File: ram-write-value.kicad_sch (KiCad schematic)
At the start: 13 parts, among them SW4 SW_DIP_x08, U31 74HCT157

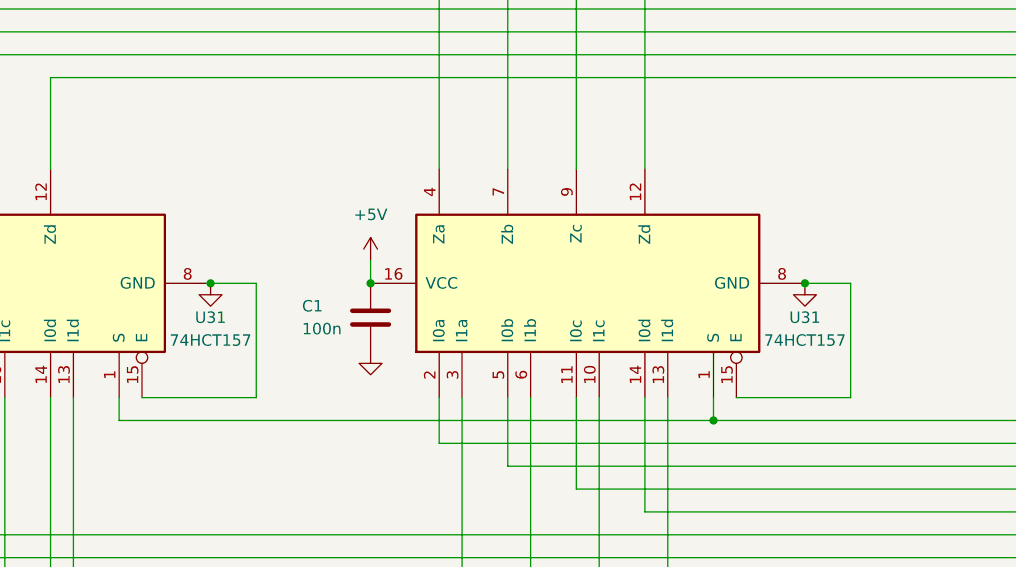
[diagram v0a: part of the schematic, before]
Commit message: added stack and x register.  Added logic for stack_address so ram address 7 gets passes and ram address 8 is high
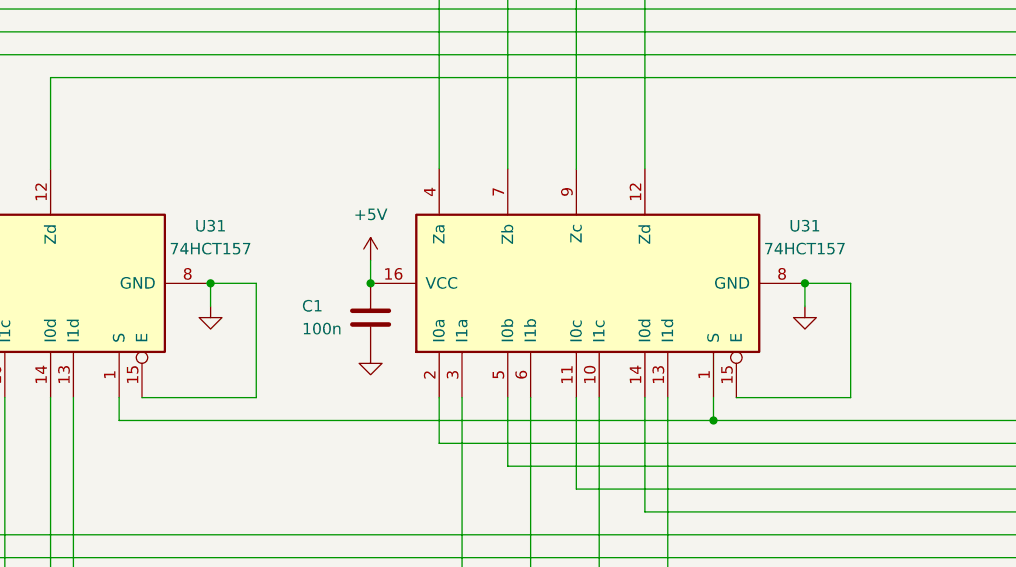
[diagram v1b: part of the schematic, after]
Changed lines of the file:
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@@
     (stroke (width 0) (type default) (color 0 0 255 1))
+  )
+  (wire (pts (xy 134.62 60.96) (xy 134.62 58.42))
+    (stroke (width 0) (type default))
+  )
+  (wire (pts (xy 200.66 60.96) (xy 200.66 58.42))
+    (stroke (width 0) (type default))
   )
   (wire (pts (xy 205.74 58.42) (xy 200.66 58.42))
@@
     )
   )
-  (symbol (lib_id "power:GND") (at 134.62 58.42 0) (unit 1)
+  (symbol (lib_id "power:GND") (at 134.62 60.96 0) (unit 1)
     (in_bom yes) (on_board yes) (dnp no) (fields_autoplaced)
-    (property "Reference" "#PWR03" (at 134.62 64.77 0)
-      (effects (font (size 1.27 1.27)) hide)
-    )
-    (property "Value" "GND" (at 134.62 63.5 0)
-      (effects (font (size 1.27 1.27)) hide)
-    )
-    (property "Footprint" "" (at 134.62 58.42 0)
-      (effects (font (size 1.27 1.27)) hide)
-    )
-    (property "Datasheet" "" (at 134.62 58.42 0)
+    (property "Reference" "#PWR03" (at 134.62 67.31 0)
+      (effects (font (size 1.27 1.27)) hide)
+    )
+    (property "Value" "GND" (at 134.62 66.04 0)
+      (effects (font (size 1.27 1.27)) hide)
+    )
+    (property "Footprint" "" (at 134.62 60.96 0)
+      (effects (font (size 1.27 1.27)) hide)
+    )
+    (property "Datasheet" "" (at 134.62 60.96 0)
       (effects (font (size 1.27 1.27)) hide)
     )
@@
   (symbol (lib_id "74xx:74LS157") (at 109.22 58.42 90) (unit 1)
     (in_bom yes) (on_board yes) (dnp no)
-    (property "Reference" "U31" (at 134.62 62.23 90)
+    (property "Reference" "U31" (at 134.62 52.07 90)
       (effects (font (size 1.27 1.27)))
     )
-    (property "Value" "74HCT157" (at 134.62 64.77 90)
+    (property "Value" "74HCT157" (at 134.62 54.61 90)
       (effects (font (size 1.27 1.27)))
     )
@@
   (symbol (lib_id "74xx:74LS157") (at 175.26 58.42 90) (unit 1)
     (in_bom yes) (on_board yes) (dnp no)
-    (property "Reference" "U31" (at 200.66 62.23 90)
+    (property "Reference" "U31" (at 200.66 52.07 90)
       (effects (font (size 1.27 1.27)))
     )
-    (property "Value" "74HCT157" (at 200.66 64.77 90)
+    (property "Value" "74HCT157" (at 200.66 54.61 90)
       (effects (font (size 1.27 1.27)))
     )
@@
     )
   )
-  (symbol (lib_id "power:GND") (at 200.66 58.42 0) (unit 1)
+  (symbol (lib_id "power:GND") (at 200.66 60.96 0) (unit 1)
     (in_bom yes) (on_board yes) (dnp no) (fields_autoplaced)
-    (property "Reference" "#PWR03" (at 200.66 64.77 0)
-      (effects (font (size 1.27 1.27)) hide)
-    )
-    (property "Value" "GND" (at 200.66 63.5 0)
-      (effects (font (size 1.27 1.27)) hide)
-    )
-    (property "Footprint" "" (at 200.66 58.42 0)
-      (effects (font (size 1.27 1.27)) hide)
-    )
-    (property "Datasheet" "" (at 200.66 58.42 0)
-      (effects (font (size 1.27 1.27)) hide)
-    )
+    (property "Reference" "#PWR03" (at 200.66 67.31 0)
+      (effects (font (size 1.27 1.27)) hide)
+    )
+    (property "Value" "GND" (at 200.66 66.04 0)
+      (effects (font (size 1.27 1.27)) hide)
+    )
+    (property "Footprint" "" (at 200.66 60.96 0)
+      (effects (font (size 1.27 1.27)) hide)
+    )
+    (property "Datasheet" "" (at 200.66 60.96 0)
+      (effects (font (size 1.27 1.27)) hide)
+    )

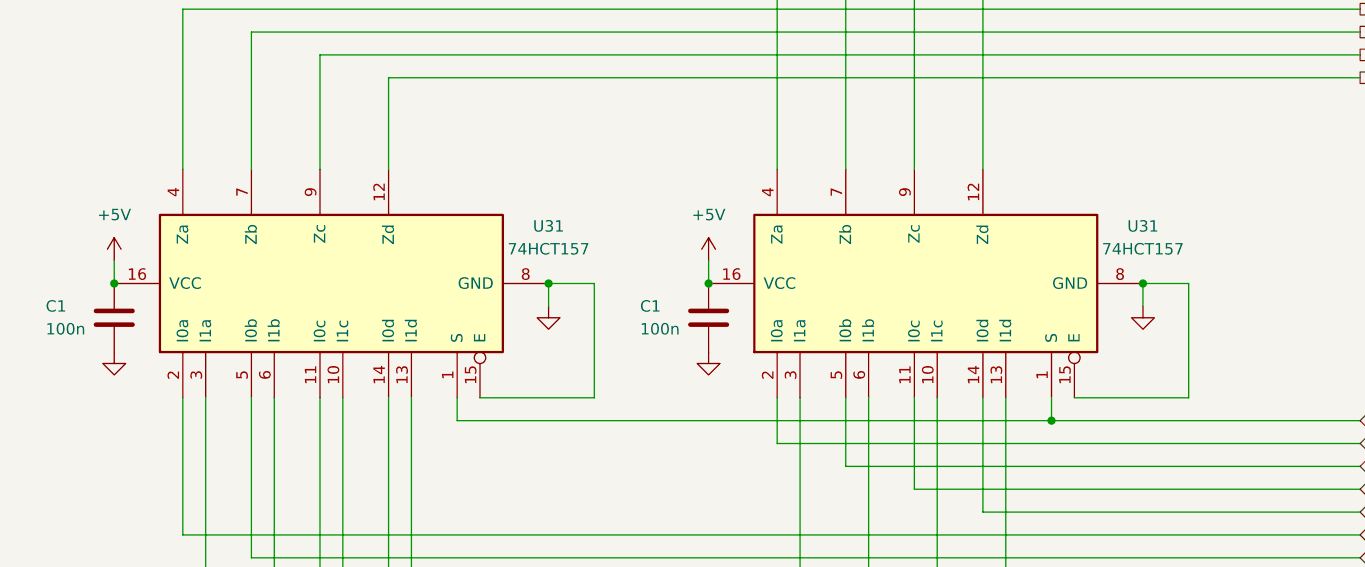
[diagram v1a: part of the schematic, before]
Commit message: changed symbols
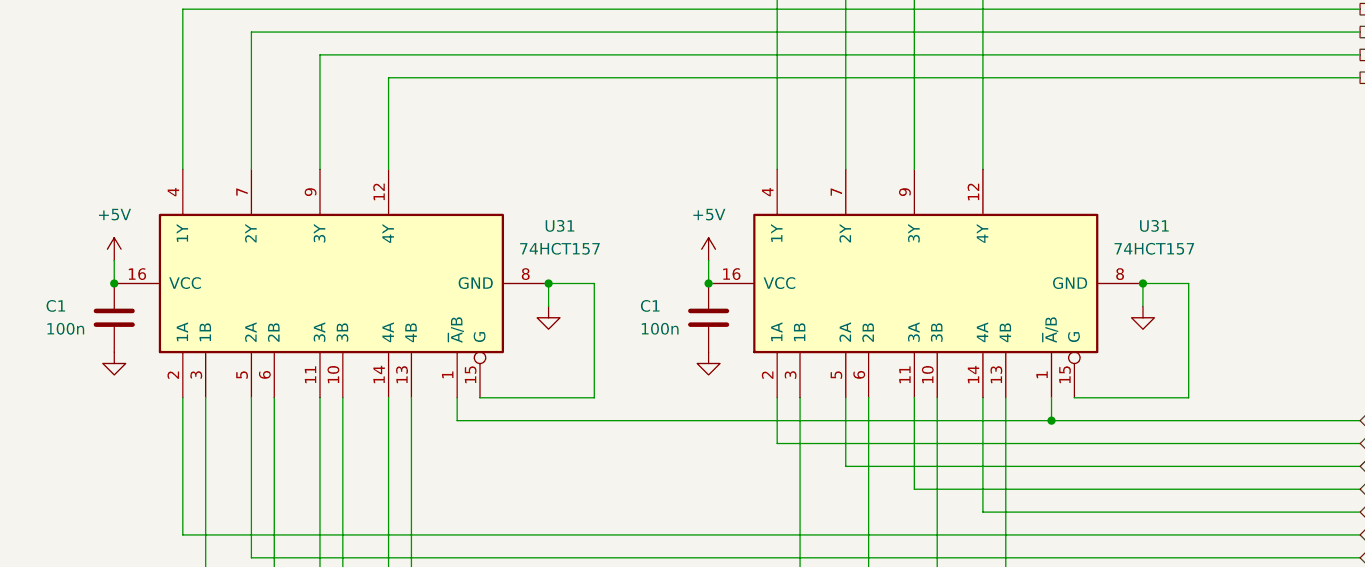
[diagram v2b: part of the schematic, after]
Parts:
- U31: symbol 74xx:74LS157 -> 01_my_library:74HCT157
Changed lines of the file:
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@@
     )
   )
-  (symbol (lib_id "74xx:74LS157") (at 109.22 58.42 90) (unit 1)
-    (in_bom yes) (on_board yes) (dnp no)
-    (property "Reference" "U31" (at 134.62 52.07 90)
-      (effects (font (size 1.27 1.27)))
-    )
-    (property "Value" "74HCT157" (at 134.62 54.61 90)
-      (effects (font (size 1.27 1.27)))
-    )
-    (property "Footprint" "Package_DIP:DIP-16_W7.62mm" (at 109.22 58.42 0)
-      (effects (font (size 1.27 1.27)) hide)
-    )
-    (property "Datasheet" "http://www.ti.com/lit/gpn/sn74LS157" (at 109.22 58.42 0)
+  (symbol (lib_id "01_my_library:74HCT157") (at 110.49 58.42 90) (unit 1)
+    (in_bom yes) (on_board yes) (dnp no)
+    (property "Reference" "U31" (at 135.89 52.07 90)
+      (effects (font (size 1.27 1.27)))
+    )
+    (property "Value" "74HCT157" (at 135.89 54.61 90)
+      (effects (font (size 1.27 1.27)))
+    )
+    (property "Footprint" "Package_DIP:DIP-16_W7.62mm" (at 110.49 57.15 0)
+      (effects (font (size 1.27 1.27)) hide)
+    )
+    (property "Datasheet" "https://www.ti.com/lit/ds/symlink/sn74hct157.pdf" (at 146.05 57.15 0)
       (effects (font (size 1.27 1.27)) hide)
     )
@@
     )
   )
-  (symbol (lib_id "74xx:74LS157") (at 175.26 58.42 90) (unit 1)
-    (in_bom yes) (on_board yes) (dnp no)
-    (property "Reference" "U31" (at 200.66 52.07 90)
-      (effects (font (size 1.27 1.27)))
-    )
-    (property "Value" "74HCT157" (at 200.66 54.61 90)
-      (effects (font (size 1.27 1.27)))
-    )
-    (property "Footprint" "Package_DIP:DIP-16_W7.62mm" (at 175.26 58.42 0)
-      (effects (font (size 1.27 1.27)) hide)
-    )
-    (property "Datasheet" "http://www.ti.com/lit/gpn/sn74LS157" (at 175.26 58.42 0)
-      (effects (font (size 1.27 1.27)) hide)
-    )
+  (symbol (lib_id "01_my_library:74HCT157") (at 176.53 58.42 90) (unit 1)
+    (in_bom yes) (on_board yes) (dnp no)
+    (property "Reference" "U31" (at 201.93 52.07 90)
+      (effects (font (size 1.27 1.27)))
+    )
+    (property "Value" "74HCT157" (at 201.93 54.61 90)
+      (effects (font (size 1.27 1.27)))
+    )
+    (property "Footprint" "Package_DIP:DIP-16_W7.62mm" (at 176.53 57.15 0)
+      (effects (font (size 1.27 1.27)) hide)
+    )
+    (property "Datasheet" "https://www.ti.com/lit/ds/symlink/sn74hct157.pdf" (at 212.09 57.15 0)
+      (effects (font (size 1.27 1.27)) hide)
+    )

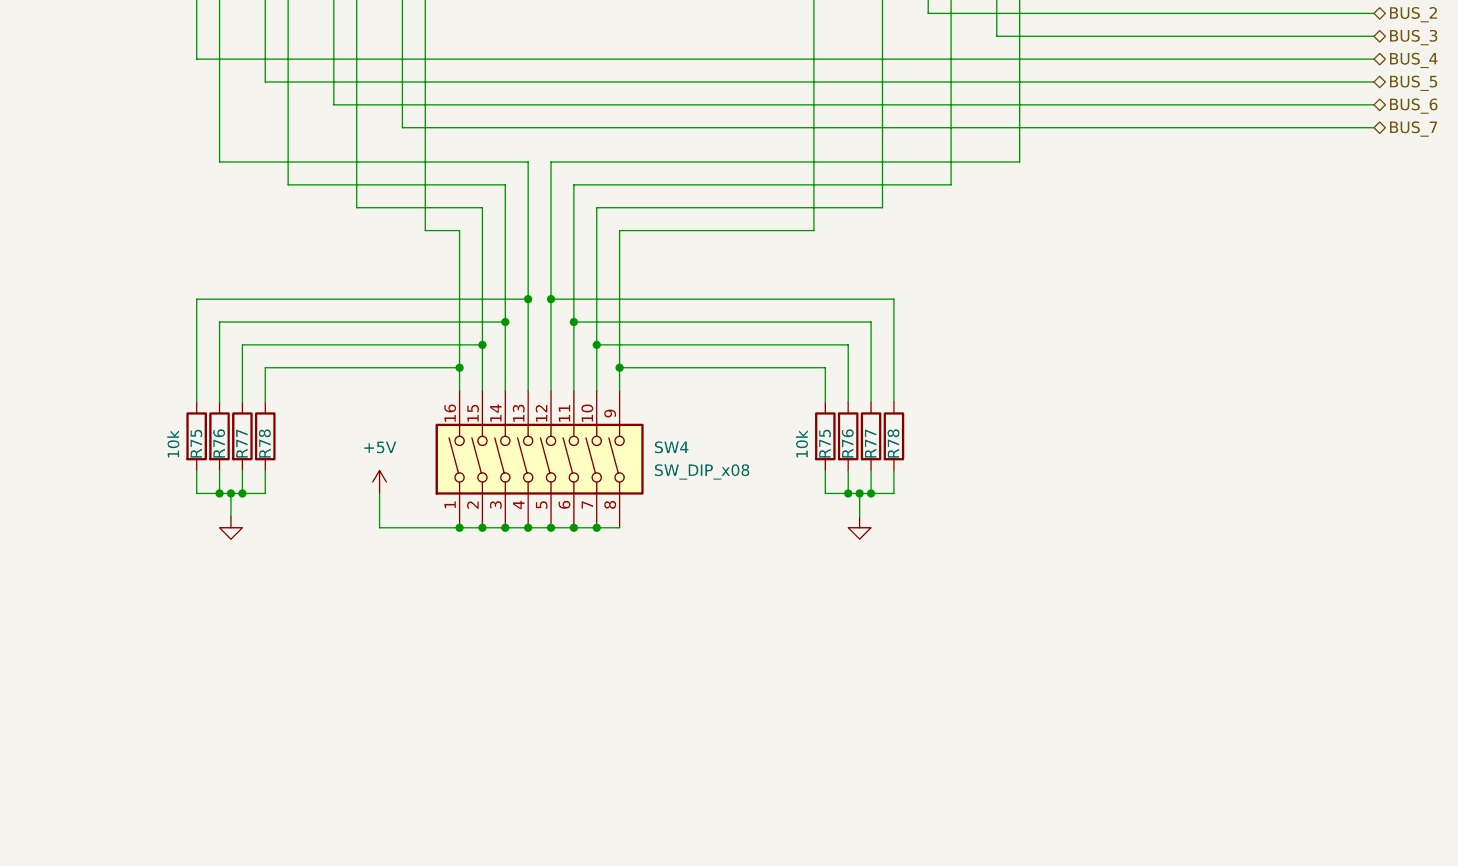
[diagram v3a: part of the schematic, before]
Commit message: add arduino headers for programming
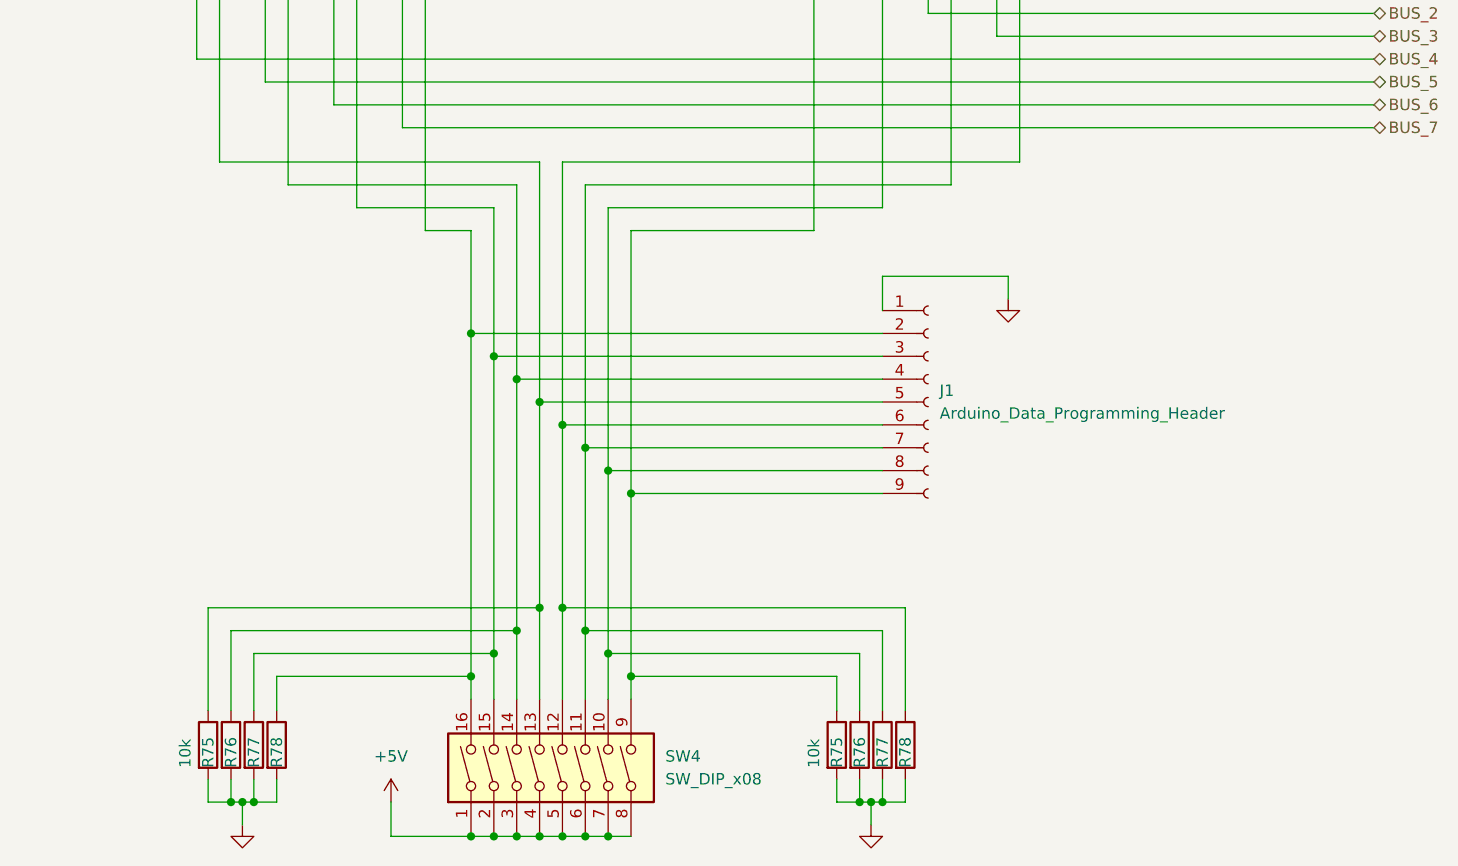
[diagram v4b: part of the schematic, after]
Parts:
- added J1: Arduino_Data_Programming_Header, Connector_PinSocket_2.54mm:PinSocket_1x09_P2.54mm_Vertical, symbol Connector:Conn_01x09_Socket
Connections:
- net GND: now also J1.1 (Pin_1)
- net at R78.1, SW4.16, U31.13 (4B): now also J1.2 (Pin_2)
- net at R76.1, SW4.10, U31.6 (2B): now also J1.8 (Pin_8)
- net at R77.1, SW4.15, U31.10 (3B): now also J1.3 (Pin_3)
- net at R75.1, SW4.13, U31.3 (1B): now also J1.5 (Pin_5)
- net at R77.1, SW4.11, U31.10 (3B): now also J1.7 (Pin_7)
- net at R75.1, SW4.9, U31.3 (1B): now also J1.9 (Pin_9)
- net at R76.1, SW4.14, U31.6 (2B): now also J1.4 (Pin_4)
- net at R78.1, SW4.12, U31.13 (4B): now also J1.6 (Pin_6)
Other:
- moved on the sheet: R75, R76, R77, R78, SW4

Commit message: kicad update
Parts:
- renumbered C1 to C33, C1 to C34, J1 to J2, R75 to R76, R76 to R77, R77 to R78, R78 to R79, R75 to R80, R76 to R81, R77 to R82, R78 to R83, U31 to U24, U31 to U25
